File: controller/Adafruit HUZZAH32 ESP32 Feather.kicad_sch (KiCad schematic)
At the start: 34 parts, among them IC1 CP2104, Q1 mmbt2222, Q2 mmbt2222, Q3 DMG3415U, SW2 KMR2, U2 AP2112-3.3, U3 MCP73831T-2ACI/OT, X1 JSTPH, X2 ESP32_WROOM32_SKINNY, X4 20329

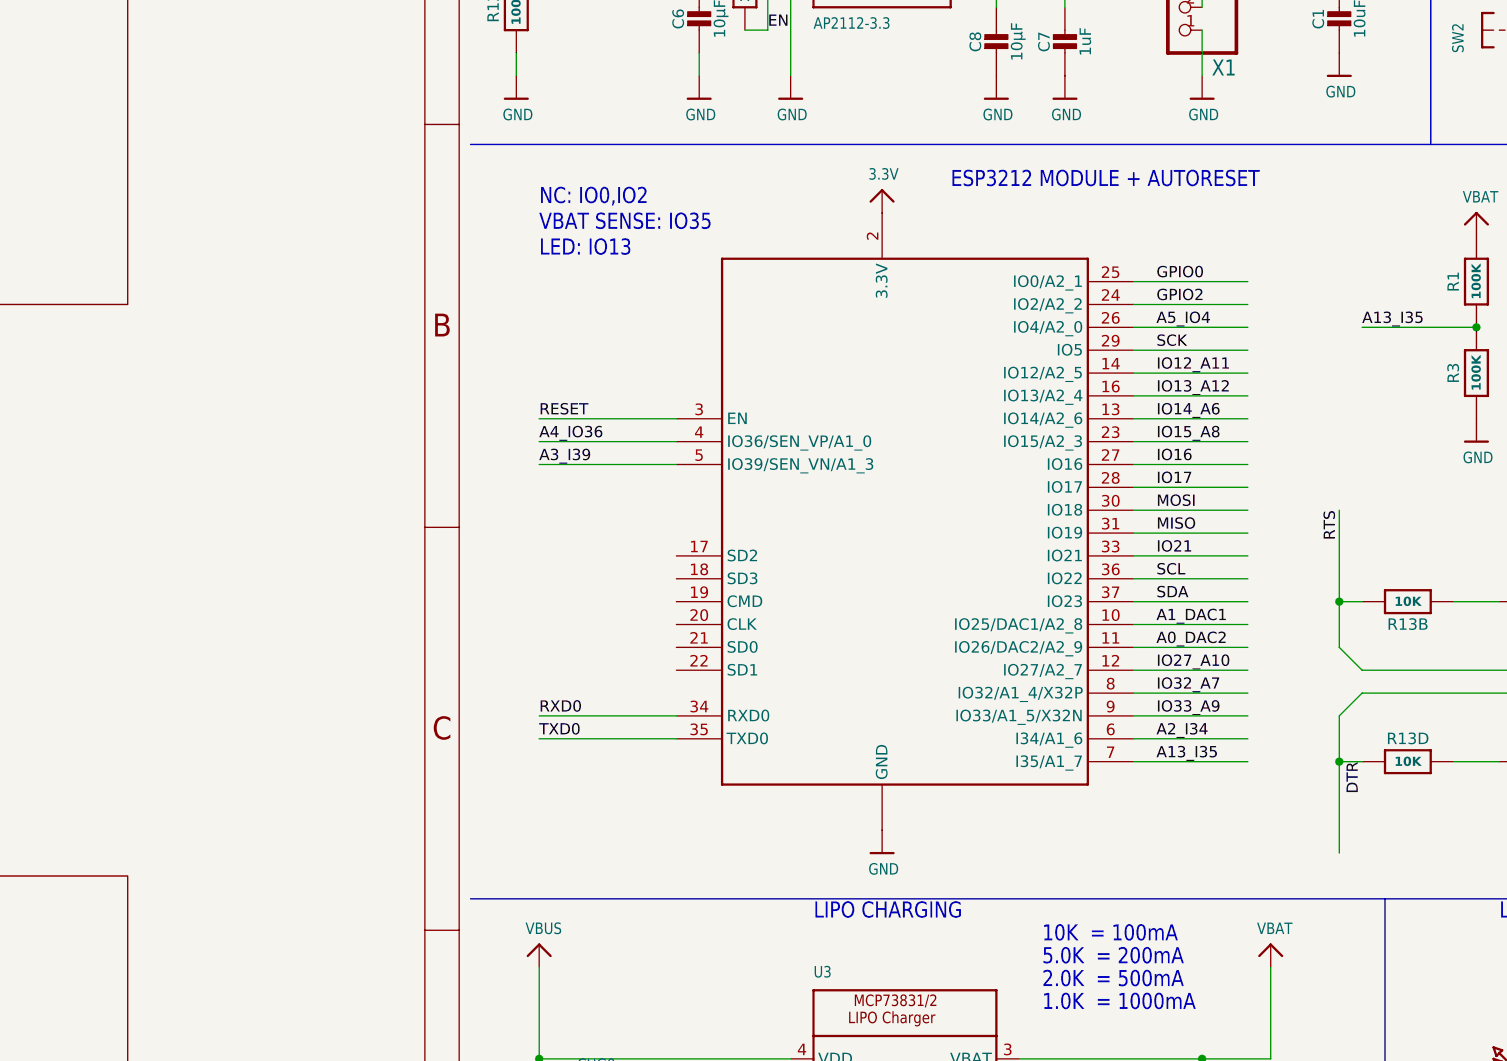
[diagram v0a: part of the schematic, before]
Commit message: Updated ESP32 SOC symbol
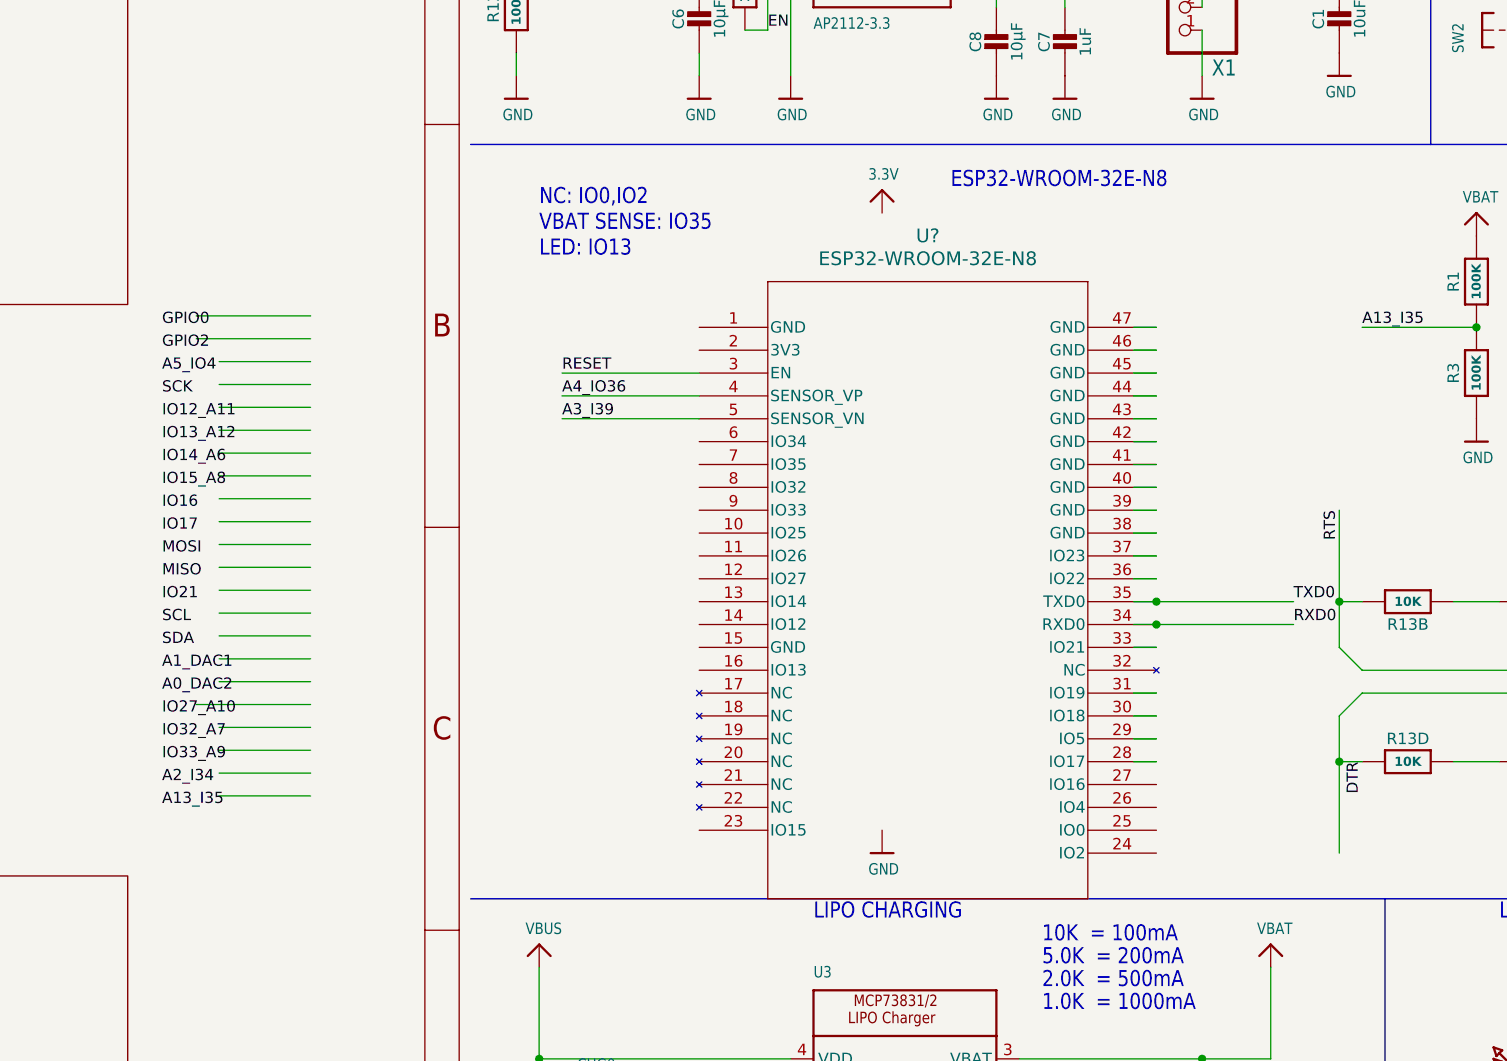
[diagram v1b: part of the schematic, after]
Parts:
- U?: renamed from X2; value ESP32_WROOM32_SKINNY -> ESP32-WROOM-32E-N8; symbol Adafruit HUZZAH32 ESP32 Feather-eagle-import:microbuilder_ESP32_WROOM32_SKINNY -> ESP32-WROOM-32E:ESP32-WROOM-32E-N8
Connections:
- net 3.3V: no longer U?.2 (3.3V)
- net A0_DAC2: no longer U?.11 (IO26/DAC2/A2_9)
- net A13_I35: no longer U?.7 (I35/A1_7)
- net A1_DAC1: no longer U?.10 (IO25/DAC1/A2_8)
- net A2_I34: no longer U?.6 (I34/A1_6)
- net A5_IO4: no longer U?.26 (IO4/A2_0)
- net GND: no longer U?.1 (GND), U?.15 (GND), U?.38 (GND), U?.P$1 (GND)
- net GPIO0: no longer U?.25 (IO0/A2_1)
- net GPIO2: no longer U?.24 (IO2/A2_2)
- net IO12_A11: no longer U?.14 (IO12/A2_5)
- net IO13_A12: no longer U?.16 (IO13/A2_4)
- net IO14_A6: no longer U?.13 (IO14/A2_6)
- net IO15_A8: no longer U?.23 (IO15/A2_3)
- net IO16: no longer U?.27 (IO16)
- net IO17: no longer U?.28 (IO17)
- net IO21: no longer U?.33 (IO21)
- net IO27_A10: no longer U?.12 (IO27/A2_7)
- net IO32_A7: no longer U?.8 (IO32/A1_4/X32P)
- net IO33_A9: no longer U?.9 (IO33/A1_5/X32N)
- net MISO: no longer U?.31 (IO19)
- net MOSI: no longer U?.30 (IO18)
- net SCK: no longer U?.29 (IO5)
- net SCL: no longer U?.36 (IO22)
- net SDA: no longer U?.37 (IO23)
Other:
- note added: "ESP32-WROOM-32E-N8"
- note removed: "ESP3212 MODULE + AUTORESET"
